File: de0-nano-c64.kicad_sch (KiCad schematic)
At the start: 51 parts, among them J1 GPIO_0, J10 SD_Card, J2 PS2_0, J3 PS2_1, J4 AUDIO_L, J5 GPIO_1, J6 VGA_OUT, J7 AUDIO_R, J8 JOYSTICK_1, J9 JOYSTICK_2

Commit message: version 1.0
initial version

---------

Co-authored-by: Marek Czerski <m.czerski@ap-tech.pl>
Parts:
- removed J4: AUDIO_L, 000_LOCAL:RCA, symbol 000_LOCAL:Conn_Coaxial
- removed J7: AUDIO_R, 000_LOCAL:RCA, symbol 000_LOCAL:Conn_Coaxial
- added J11: AUDIO, 000_LOCAL:Jack_3.5mm_CUI_SJ1-3523N_Horizontal, symbol 000_LOCAL:AudioJack3
- J10: footprint Connector_Card:microSD_HC_Hirose_DM3AT-SF-PEJM5 -> 000_LOCAL:MOLEX_503398-1892; symbol Connector:Micro_SD_Card -> 000_LOCAL:Micro_SD_Card
- J2, J3: symbol Connector:DIN-6 -> 000_LOCAL:Mini-DIN-6
- J6: value VGA_OUT -> VGA; footprint 000_LOCAL:HD15-SN-25 -> 000_LOCAL:AMPHENOL_ICD15S13E4GV00LF
- J8, J9: footprint Connector_Dsub:DSUB-9_Male_Horizontal_P2.77x2.84mm_EdgePinOffset4.94mm_Housed_MountingHolesOffset7.48mm -> Connector_Dsub:DSUB-9_Male_Horizontal_P2.77x2.84mm_EdgePinOffset7.70mm_Housed_MountingHolesOffset9.12mm; symbol Connector:DE9_Plug_MountingHoles -> 000_LOCAL:DE9_Plug_MountingHoles
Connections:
- net GND: now also J2.S1, J3.S1, J11.S
- net J1_DOWN: now also J5.13 (Pin_13); no longer J5.3 (Pin_3)
- net J1_FIRE: now also J5.5 (Pin_5); no longer J5.9 (Pin_9)
- net J1_LEFT: now also J5.9 (Pin_9); no longer J5.5 (Pin_5)
- net J1_UP: now also J5.15 (Pin_15); no longer J5.1 (Pin_1)
- net J2_DOWN: now also J5.23 (Pin_23); no longer J5.15 (Pin_15)
- net J2_FIRE: now also J5.17 (Pin_17); no longer J5.21 (Pin_21)
- net J2_LEFT: now also J5.21 (Pin_21); no longer J5.17 (Pin_17)
- net J2_UP: now also J5.25 (Pin_25); no longer J5.13 (Pin_13)
- net PS2_0_CLK: now also J5.36 (Pin_36); no longer J5.38 (Pin_38)
- net PS2_0_DAT: now also J5.34 (Pin_34); no longer J5.40 (Pin_40)
- net PS2_1_CLK: now also J5.40 (Pin_40); no longer J5.34 (Pin_34)
- net PS2_1_DAT: now also J5.38 (Pin_38); no longer J5.36 (Pin_36)
- net PWM_L: now also J5.1 (Pin_1); no longer J5.23 (Pin_23)
- net PWM_R: now also J5.3 (Pin_3); no longer J5.25 (Pin_25)
- net SD_CLK: now also J5.39 (Pin_39); no longer J5.37 (Pin_37)
- net SD_CMD: now also J5.33 (Pin_33); no longer J5.39 (Pin_39)
- net SD_DAT0: now also J5.31 (Pin_31); no longer J5.27 (Pin_27)
- net SD_DAT1: now also J5.27 (Pin_27); no longer J5.31 (Pin_31)
- net SD_DAT2: now also J5.37 (Pin_37); no longer J5.33 (Pin_33)
- net at C1.1, R22.2: now also J11.T
- net at C2.1, R23.2: now also J11.R
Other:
- moved on the sheet: R17, R19

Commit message: reorder some pins due to input only problem
audio PWM_L/R were assigne to input only pins
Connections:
- net J1_FIRE: now also J5.3 (Pin_3); no longer J5.5 (Pin_5)
- net J1_RIGHT: now also J5.1 (Pin_1); no longer J5.7 (Pin_7)
- net PWM_L: now also J5.5 (Pin_5); no longer J5.1 (Pin_1)
- net PWM_R: now also J5.7 (Pin_7); no longer J5.3 (Pin_3)
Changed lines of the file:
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@@
     (effects (font (size 1.27 1.27)) (justify left bottom))
   )
-  (label "J1_RIGHT" (at 93.98 39.37 180) (fields_autoplaced)
+  (label "PWM_R" (at 93.98 39.37 180) (fields_autoplaced)
     (effects (font (size 1.27 1.27)) (justify right bottom))
   )
@@
     (effects (font (size 1.27 1.27)) (justify right bottom))
   )
-  (label "J1_FIRE" (at 93.98 36.83 180) (fields_autoplaced)
+  (label "PWM_L" (at 93.98 36.83 180) (fields_autoplaced)
     (effects (font (size 1.27 1.27)) (justify right bottom))
   )
@@
     (effects (font (size 1.27 1.27)) (justify left bottom))
   )
-  (label "PWM_R" (at 93.98 34.29 180) (fields_autoplaced)
+  (label "J1_FIRE" (at 93.98 34.29 180) (fields_autoplaced)
     (effects (font (size 1.27 1.27)) (justify right bottom))
   )
@@
     (effects (font (size 1.27 1.27)) (justify left bottom))
   )
-  (label "PWM_L" (at 93.98 31.75 180) (fields_autoplaced)
+  (label "J1_RIGHT" (at 93.98 31.75 180) (fields_autoplaced)
     (effects (font (size 1.27 1.27)) (justify right bottom))
   )

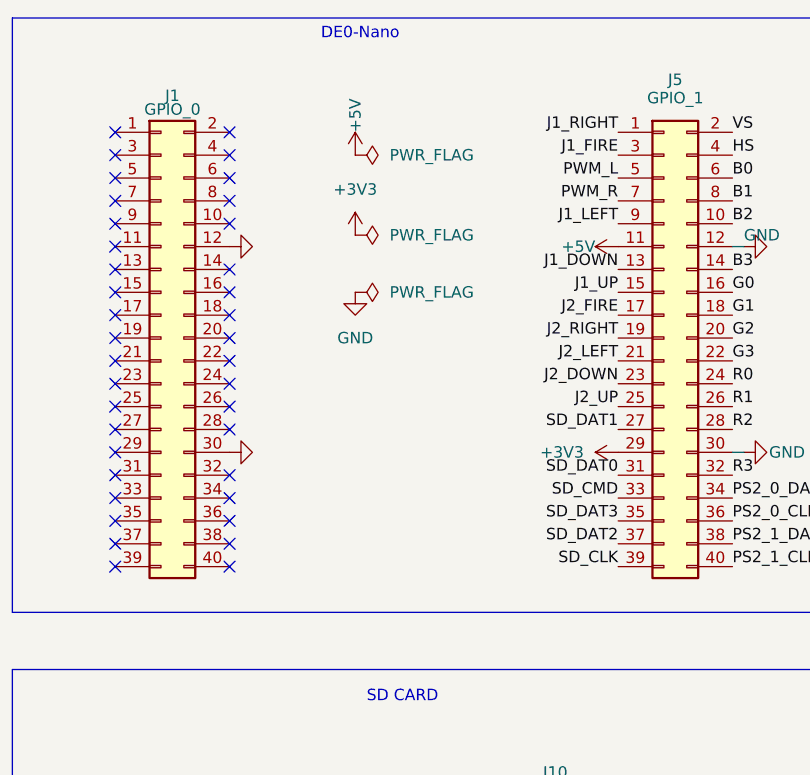
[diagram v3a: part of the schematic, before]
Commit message: add USB socket for power + add whole cut for dip switches
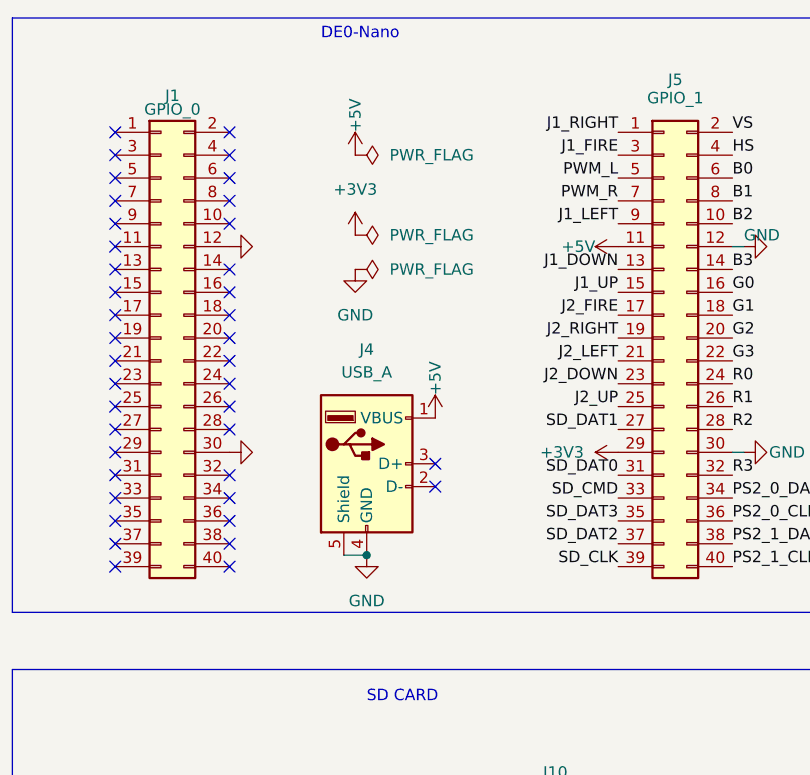
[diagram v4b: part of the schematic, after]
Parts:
- added J4: USB_A, Connector_USB:USB_A_Molex_67643_Horizontal, symbol Connector:USB_A
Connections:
- net +5V: now also J4.1 (VBUS)
- net GND: now also J4.4 (GND), J4.5 (Shield)
- no-connect marks 50 -> 52
